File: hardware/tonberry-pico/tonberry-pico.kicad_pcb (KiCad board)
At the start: 2 copper layers, 98 x 53.5 mm, 31 parts, among them J1 MicroSD_Breakout, J2 SparkFun I2S Audio Breakout M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, J3 RC522_Breakout, J4 Adafruit_bq25185_5V, J5 UART, J6 WS2812, J7 Buttons, J8 Conn_01x01, Q1 2N7000, Q2 2N7000, SW5 SW_Push, U1 RaspberryPi_Pico_W

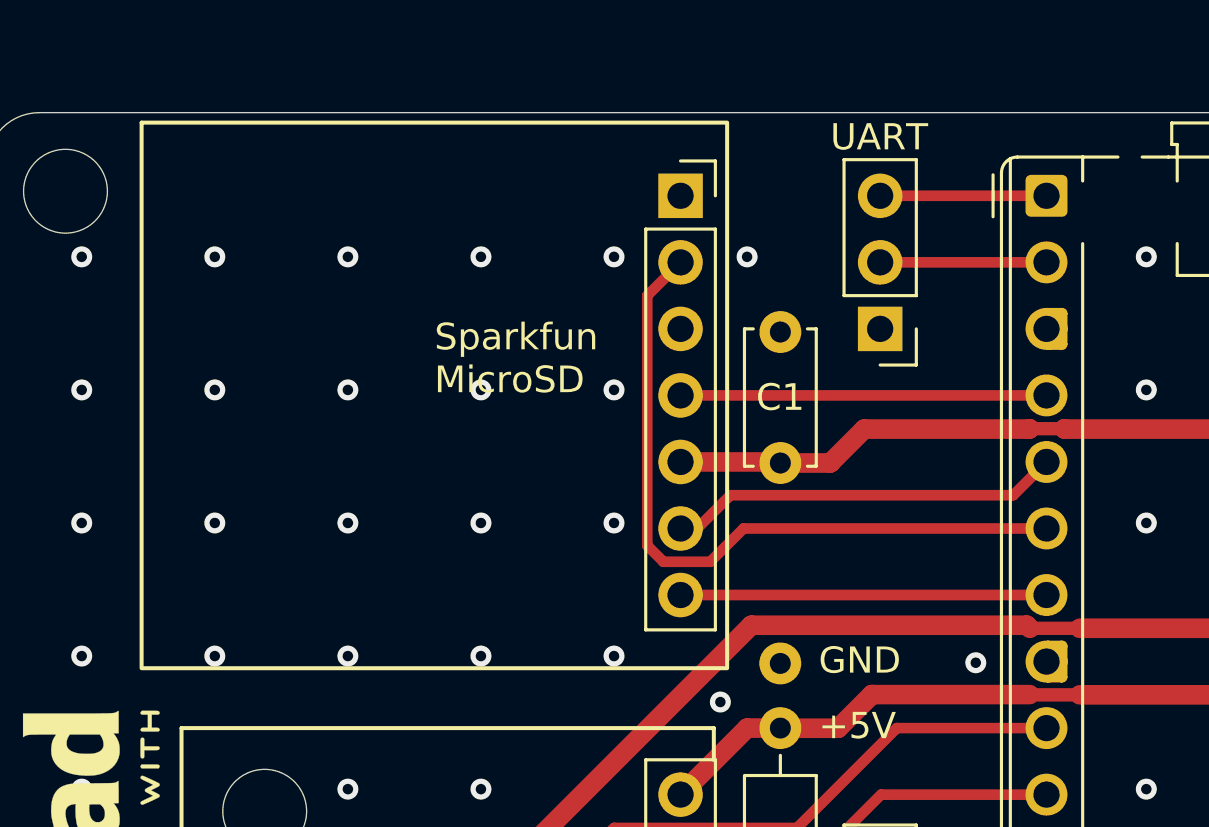
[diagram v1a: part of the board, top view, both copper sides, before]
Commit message: this adds the footprint of the microSD card socket (same as sparkfun_microSD_Transflash_Breakout) so that it could be used optionally, since the original sparkfun_microSD_Transflash_Breakout is not available anymore. This part is just about manually solderable, the chips on the other breakout boards maybe less so. Let's order this and see how it fares :)
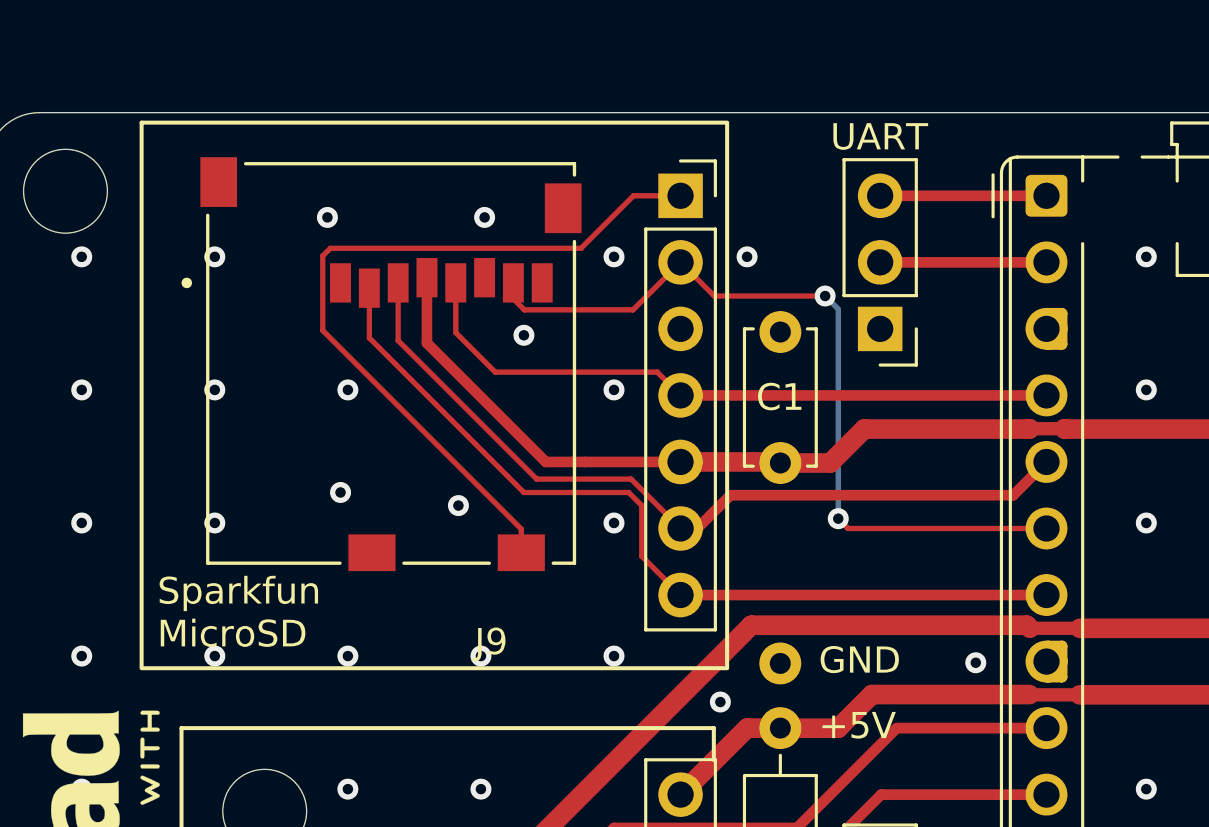
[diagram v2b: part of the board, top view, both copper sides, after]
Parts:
- added J9: MSD-6-A, MSD-6-A:CUI_MSD-6-A, F.Cu at (133.7, 47.7)
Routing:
- net /SD_CD: track 0.00 -> 29.1 mm
- net /SD_CS: track 14.0 -> 32.9 mm
- net /SD_DI: track 15.0 -> 31.0 mm
- net +3V3: track 102.3 -> 116.3 mm
- net /SD_SCK: track 14.0 -> 25.4 mm
- net /SD_DO: track 27.4 -> 30.8 mm, vias 0 -> 2
